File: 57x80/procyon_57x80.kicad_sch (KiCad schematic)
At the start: 34 parts, among them J1 Conn_01x07_Pin, Q1 AO3401A, U1 mXT336UD-MAU002

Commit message: A bit more documentation.
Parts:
- added SW1: SW_Push, Button_Switch_SMD:SW_SPST_EVQQ2, symbol Switch:SW_Push
- added TP10, TP9: TestPoint, TestPoint:TestPoint_Pad_D1.0mm, symbol Connector:TestPoint
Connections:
- net GND: now also SW1.2
- net GPIO3: now reaches U1.42 (GPIO3)
- net GPIO3: now also TP9.1
- net GPIO4: now reaches U1.43 (GPIO4)
- net GPIO4: now also SW1.1, TP10.1
- no-connect marks 10 -> 8
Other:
- note added: "Optional Button"

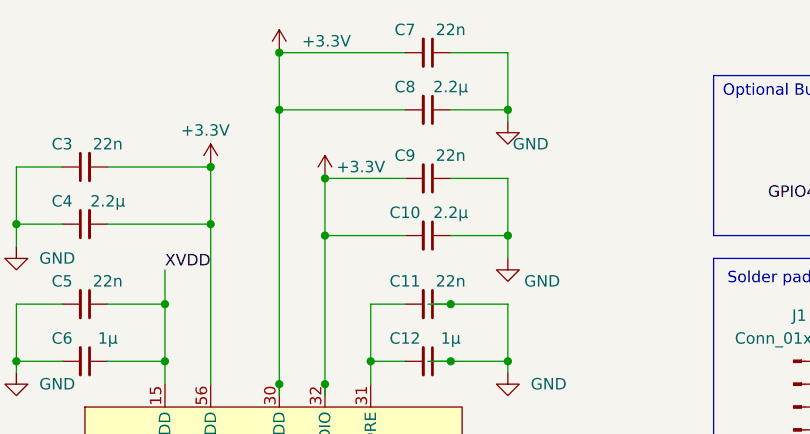
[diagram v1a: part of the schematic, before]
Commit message: Add missing rule areas. Attempt to reduce paracitic capacitance.
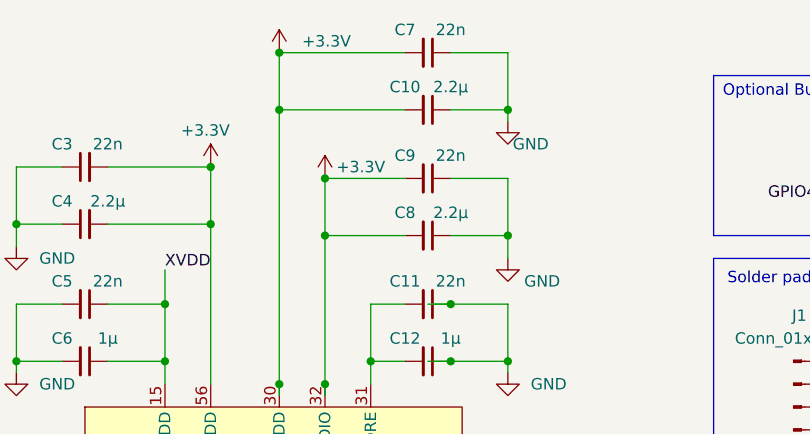
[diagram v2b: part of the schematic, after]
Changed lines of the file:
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@@
-	)
-	(symbol
-		(lib_id "Device:C_Small")
-		(at 124.46 30.48 270)
-		(unit 1)
-		(exclude_from_sim no)
-		(in_bom yes)
-		(on_board yes)
-		(dnp no)
-		(property "Reference" "C8"
-			(at 121.92 27.94 90)
-			(effects
-				(font
-					(size 1.27 1.27)
-				)
-			)
-		)
-		(property "Value" "2.2µ"
-			(at 127 27.94 90)
-			(effects
-				(font
-					(size 1.27 1.27)
-				)
-			)
-		)
-		(property "Footprint" "Capacitor_SMD:C_0603_1608Metric"
-			(at 124.46 30.48 0)
-			(effects
-				(font
-					(size 1.27 1.27)
-				)
-				(hide yes)
-			)
-		)
-		(property "Datasheet" "~"
-			(at 124.46 30.48 0)
-			(effects
-				(font
-					(size 1.27 1.27)
-				)
-				(hide yes)
-			)
-		)
-		(property "Description" ""
-			(at 124.46 30.48 0)
-			(effects
-				(font
-					(size 1.27 1.27)
-				)
-				(hide yes)
-			)
-		)
-		(property "LCSC" "C23630"
-			(at 121.92 27.94 0)
-			(effects
-				(font
-					(size 1.27 1.27)
-				)
-				(hide yes)
-			)
-		)
-		(pin "1"
-		)
-		(pin "2"
-		)
-		(instances
-			(project ""
-				(path "/22e83c18-ea75-4c5e-9dba-5c9f658130b9"
-					(reference "C8")
-					(unit 1)
-				)
-			)
-			(project "trackpad"
-				(path "/3796446b-0052-4d89-b512-07a2e9135d0d/2780c9a8-e5e0-42e8-93d7-9eb6f8aa439b"
-					(reference "C26")
-					(unit 1)
-				)
-			)
-		)
 	)
 	(symbol
@@
 	)
 	(symbol
+		(lib_id "Device:C_Small")
+		(at 124.46 44.45 270)
+		(unit 1)
+		(exclude_from_sim no)
+		(in_bom yes)
+		(on_board yes)
+		(dnp no)
+		(property "Reference" "C8"
+			(at 121.92 41.91 90)
+			(effects
+				(font
+					(size 1.27 1.27)
+				)
+			)
+		)
+		(property "Value" "2.2µ"
+			(at 127 41.91 90)
+			(effects
+				(font
+					(size 1.27 1.27)
+				)
+			)
+		)
+		(property "Footprint" "Capacitor_SMD:C_0603_1608Metric"
+			(at 124.46 44.45 0)
+			(effects
+				(font
+					(size 1.27 1.27)
+				)
+				(hide yes)
+			)
+		)
+		(property "Datasheet" "~"
+			(at 124.46 44.45 0)
+			(effects
+				(font
+					(size 1.27 1.27)
+				)
+				(hide yes)
+			)
+		)
+		(property "Description" ""
+			(at 124.46 44.45 0)
+			(effects
+				(font
+					(size 1.27 1.27)
+				)
+				(hide yes)
+			)
+		)
+		(property "LCSC" "C23630"
+			(at 121.92 41.91 0)
+			(effects
+				(font
+					(size 1.27 1.27)
+				)
+				(hide yes)
+			)
+		)
+		(pin "1"
+		)
+		(pin "2"
+		)
+		(instances
+			(project "procyon_57x80"
+				(path "/22e83c18-ea75-4c5e-9dba-5c9f658130b9"
+					(reference "C8")
+					(unit 1)
+				)
+			)
+		)
+	)
+	(symbol
 		(lib_id "power:+3V3")
 		(at 242.57 101.6 90)
@@
 	)
 	(symbol
-		(lib_id "Device:C_Small")
-		(at 124.46 44.45 270)
-		(unit 1)
-		(exclude_from_sim no)
-		(in_bom yes)
-		(on_board yes)
-		(dnp no)
-		(property "Reference" "C10"
-			(at 121.92 41.91 90)
-			(effects
-				(font
-					(size 1.27 1.27)
-				)
-			)
-		)
-		(property "Value" "2.2µ"
-			(at 127 41.91 90)
-			(effects
-				(font
-					(size 1.27 1.27)
-				)
-			)
-		)
-		(property "Footprint" "Capacitor_SMD:C_0603_1608Metric"
-			(at 124.46 44.45 0)
-			(effects
-				(font
-					(size 1.27 1.27)
-				)
-				(hide yes)
-			)
-		)
-		(property "Datasheet" "~"
-			(at 124.46 44.45 0)
-			(effects
-				(font
-					(size 1.27 1.27)
-				)
-				(hide yes)
-			)
-		)
-		(property "Description" ""
-			(at 124.46 44.45 0)
-			(effects
-				(font
-					(size 1.27 1.27)
-				)
-				(hide yes)
-			)
-		)
-		(property "LCSC" "C23630"
-			(at 121.92 41.91 0)
-			(effects
-				(font
-					(size 1.27 1.27)
-				)
-				(hide yes)
-			)
-		)
-		(pin "1"
-		)
-		(pin "2"
-		)
-		(instances
-			(project ""
-				(path "/22e83c18-ea75-4c5e-9dba-5c9f658130b9"
-					(reference "C10")
-					(unit 1)
-				)
-			)
-			(project "trackpad"
-				(path "/3796446b-0052-4d89-b512-07a2e9135d0d/2780c9a8-e5e0-42e8-93d7-9eb6f8aa439b"
-					(reference "C24")
-					(unit 1)
-				)
-			)
-		)
-	)
-	(symbol
 		(lib_id "power:GND2")
 		(at 171.45 160.02 90)
@@
 					(unit 1)
 				)
+			)
+		)
+	)
+	(symbol
+		(lib_id "Device:C_Small")
+		(at 124.46 30.48 270)
+		(unit 1)
+		(exclude_from_sim no)
+		(in_bom yes)
+		(on_board yes)
+		(dnp no)
+		(property "Reference" "C10"
+			(at 121.92 27.94 90)
+			(effects
+				(font
+					(size 1.27 1.27)
+				)
+			)
+		)
+		(property "Value" "2.2µ"
+			(at 127 27.94 90)
+			(effects
+				(font
+					(size 1.27 1.27)
+				)
+			)
+		)
+		(property "Footprint" "Capacitor_SMD:C_0603_1608Metric"
+			(at 124.46 30.48 0)
+			(effects
+				(font
+					(size 1.27 1.27)
+				)
+				(hide yes)
+			)
+		)
+		(property "Datasheet" "~"
+			(at 124.46 30.48 0)
+			(effects
+				(font
+					(size 1.27 1.27)
+				)
+				(hide yes)
+			)
+		)
+		(property "Description" ""
+			(at 124.46 30.48 0)
+			(effects
+				(font
+					(size 1.27 1.27)
+				)
+				(hide yes)
+			)
+		)
+		(property "LCSC" "C23630"
+			(at 121.92 27.94 0)
+			(effects
+				(font
+					(size 1.27 1.27)
+				)
+				(hide yes)
+			)
+		)
+		(pin "1"
+		)
+		(pin "2"
+		)
+		(instances
+			(project "procyon_57x80"
+				(path "/22e83c18-ea75-4c5e-9dba-5c9f658130b9"
+					(reference "C10")
+					(unit 1)
+				)
